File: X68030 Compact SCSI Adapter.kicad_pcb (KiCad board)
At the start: 2 copper layers, 28.8 x 85.3 mm, 5 parts, among them J1 X68030 Internal SCSI Connector, J2 DB25_Plug_MountingHoles

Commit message: Rev 1.0 - verified to fit
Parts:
- removed the G*** at (44.5, 63.8)
- removed the G*** at (39.7, 98.8)
- added G***: LOGO, LOGO, B.Cu at (40.9, 92.2)
- moved J2 14.5 mm to (50.4, 56.0)
- moved G*** 14.4 mm to (38.1, 90.4)
- moved J1 0.40 mm to (37.1, 31.0)
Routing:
- net GND: track 176.3 -> 50.3 mm
- net DB0: track 80.5 -> 49.1 mm, vias 1 -> 0
- net DB1: track 79.7 -> 52.2 mm, vias 1 -> 0
- net DB2: track 78.9 -> 52.2 mm, vias 1 -> 0
- net REQ: track 28.3 -> 53.8 mm, vias 0 -> 1
- net DB3: track 74.5 -> 49.2 mm
- net RST: track 29.0 -> 53.8 mm
- net CD: track 27.2 -> 51.9 mm, vias 0 -> 1
- net IO: track 28.1 -> 52.4 mm
- net DB4: track 75.5 -> 52.1 mm
- net MSG: track 27.7 -> 50.5 mm, vias 0 -> 1
- net SEL: track 28.7 -> 50.4 mm, vias 0 -> 1
- net ACK: track 31.0 -> 52.0 mm
- net DB6: track 69.9 -> 52.0 mm
- net DB5: track 71.0 -> 53.9 mm
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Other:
- board size 28.8 x 85.3 mm -> 26.9 x 71.1 mm

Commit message: Fabricated
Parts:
- moved J1 58.6 mm to (95.6, 34.7), turned to 90 degrees
- moved G*** 54.8 mm to (36.2, 35.7), turned to 0 degrees
- moved G*** 54.1 mm to (34.4, 38.4), turned to 180 degrees
- moved J2 21.7 mm to (70.6, 48.0), turned to 0 degrees
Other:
- board size 26.9 x 71.1 mm -> 71.1 x 26.9 mm

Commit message: Rev 2.0
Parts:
- moved G*** 0.78 mm to (35.1, 38.9)
- moved G*** 0.74 mm to (35.6, 36.1)
- moved J1 0.37 mm to (95.5, 35.1)
- moved J2 0.37 mm to (70.6, 48.3)
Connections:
- J1 pad 1: GND -> unconnected-(J1-Pin_1-Pad1)
- J1 pad 10: DB4 -> unconnected-(J1-Pin_10-Pad10)
- J1 pad 11: GND -> VCC
- J1 pad 12: DB5 -> VCC
- J1 pad 14: DB6 -> GND
- J1 pad 16: DB7 -> DB0
- J1 pad 18: DBP -> DB1
- J1 pad 2: DB0 -> unconnected-(J1-Pin_2-Pad2)
- J1 pad 20: GND -> DB2
- J1 pad 22: GND -> DB3
- J1 pad 24: GND -> DB4
- J1 pad 25: unconnected-(J1-Pin_25-Pad25) -> GND
- J1 pad 26: +5V -> DB5
- J1 pad 27: GND -> unconnected-(J1-Pin_27-Pad27)
- J1 pad 28: GND -> DB6
- J1 pad 3: GND -> unconnected-(J1-Pin_3-Pad3)
- J1 pad 30: GND -> DB7
- J1 pad 32: ATN -> DBP
- J1 pad 34: GND -> TMPWR
- J1 pad 35: GND -> ATN
- J1 pad 39: GND -> RST
- J1 pad 4: DB1 -> unconnected-(J1-Pin_4-Pad4)
- J1 pad 40: RST -> MSG
- J1 pad 42: MSG -> SEL
- J1 pad 43: GND -> IO
- J1 pad 44: SEL -> CD
- J1 pad 46: CD -> REQ
- J1 pad 48: REQ -> GND
- J1 pad 49: GND -> VCC
- J1 pad 5: GND -> ID1
- J1 pad 50: IO -> VCC
- J1 pad 6: DB2 -> ID2
- J1 pad 7: GND -> ID4
- J1 pad 8: DB3 -> HD LED
- J1 pad 9: GND -> unconnected-(J1-Pin_9-Pad9)
- J2 pad 25: +5V -> VCC
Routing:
- net VCC: track 0.00 -> 69.5 mm
- net +5V: track 52.2 -> 0.00 mm
- net GND: track 50.3 -> 75.6 mm
- net REQ: track 53.8 -> 40.4 mm, vias 1 -> 0
- net ACK: track 52.0 -> 40.3 mm
- net IO: track 52.4 -> 41.9 mm, vias 0 -> 1
- net RST: track 53.8 -> 43.2 mm, vias 0 -> 2
- net DB5: track 53.9 -> 43.4 mm, vias 1 -> 0
- net MSG: track 50.5 -> 40.1 mm
- net BSY: track 52.9 -> 42.9 mm
- net DB7: track 53.5 -> 43.5 mm
- net CD: track 51.9 -> 42.1 mm, vias 1 -> 2
- net DB1: track 52.2 -> 43.2 mm
- net DB2: track 52.2 -> 43.4 mm
- net DB4: track 52.1 -> 43.3 mm, vias 1 -> 0
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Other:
- board size 71.1 x 26.9 mm -> 71.1 x 26.4 mm
- board text added: "Rev 2.0"
- board text removed: "Rev 1.0"

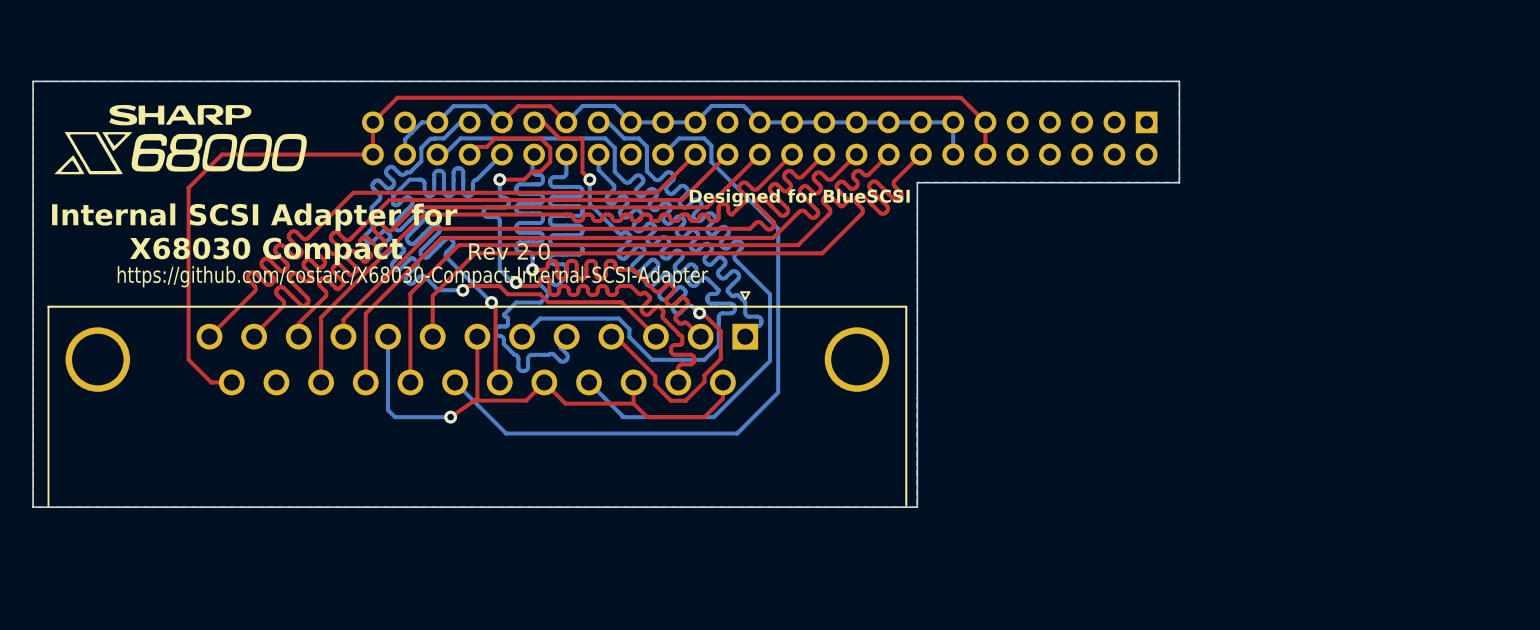
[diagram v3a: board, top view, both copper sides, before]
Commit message: Fabricated Rev 2.0 with pinout based on CZ-147 Service Manual for X68030 Compact
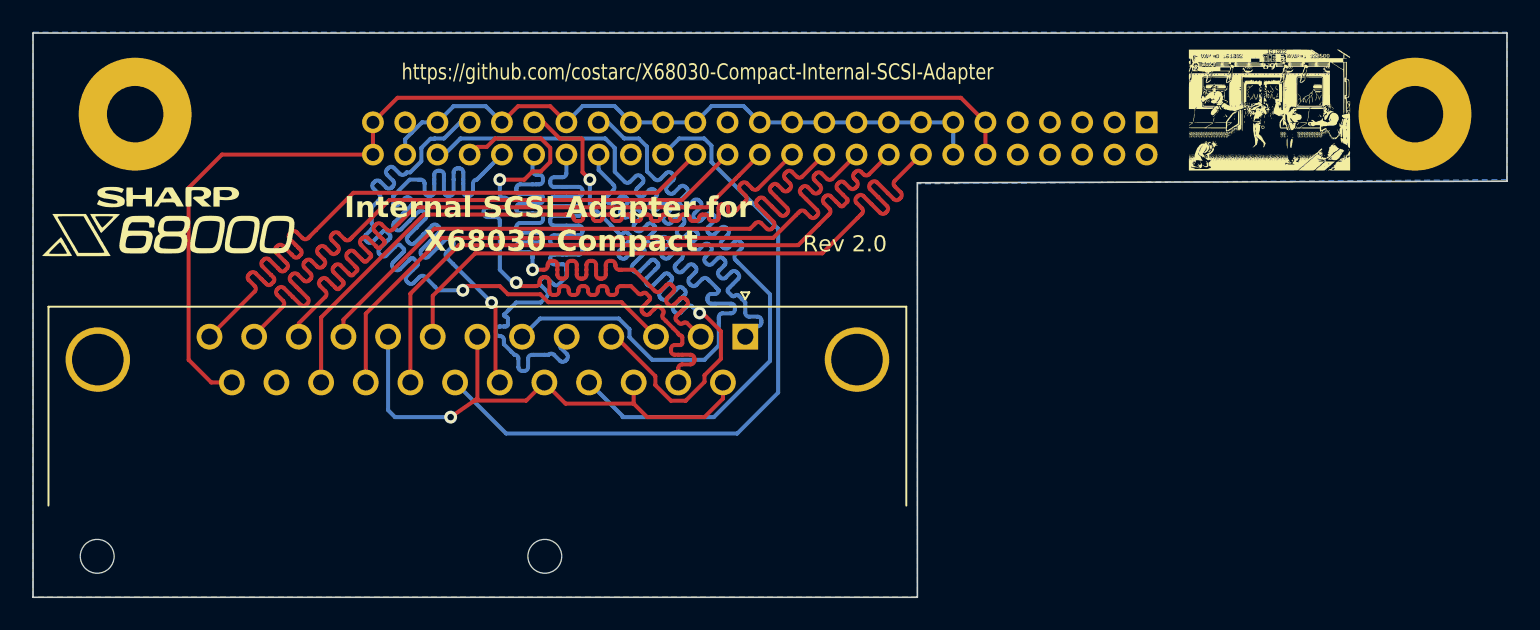
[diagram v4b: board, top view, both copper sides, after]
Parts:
- added H1: MountingHole, MountingHole:MountingHole_3.5mm_Pad, F.Cu at (112.2, 34.5)
- added H2: MountingHole, MountingHole:MountingHole_3.5mm_Pad, F.Cu at (32.8, 34.5)
- added H3: MountingHole, MountingHole:MountingHole_2.1mm, F.Cu at (30.4, 62.0)
- added H4: MountingHole, MountingHole:MountingHole_2.1mm, F.Cu at (58.2, 62.0)
- G***: moved to F.Cu
- moved G*** 68.2 mm to (103.1, 34.3), turned to 0 degrees
- moved G*** 5.14 mm to (34.8, 41.1)
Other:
- board size 71.1 x 26.4 mm -> 91.4 x 35 mm
- board text removed: "Designed for BlueSCSI"
